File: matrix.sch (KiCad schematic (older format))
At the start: 134 parts, among them SW1 SW_Push, SW10 SW_Push, SW11 SW_Push, SW12 SW_Push, SW13 SW_Push, SW14 SW_Push, SW15 SW_Push, SW16 SW_Push, SW17 SW_Push, SW18 SW_Push, SW19 SW_Push, SW2 SW_Push, SW20 SW_Push, SW21 SW_Push, SW22 SW_Push, SW23 SW_Push, SW24 SW_Push, SW25 SW_Push, SW26 SW_Push, SW27 SW_Push, SW28 SW_Push, SW29 SW_Push, SW3 SW_Push, SW30 SW_Push, SW31 SW_Push, SW32 SW_Push, SW33 SW_Push, SW34 SW_Push, SW35 SW_Push, SW36 SW_Push, SW37 SW_Push, SW38 SW_Push, SW39 SW_Push, SW4 SW_Push, SW40 SW_Push, SW41 SW_Push, SW42 SW_Push, SW43 SW_Push, SW44 SW_Push, SW45 SW_Push, SW46 SW_Push, SW47 SW_Push, SW48 SW_Push, SW49 SW_Push, SW5 SW_Push, SW50 SW_Push, SW51 SW_Push, SW52 SW_Push, SW53 SW_Push, SW54 SW_Push, SW55 SW_Push, SW56 SW_Push, SW57 SW_Push, SW58 SW_Push, SW59 SW_Push, SW6 SW_Push, SW60 SW_Push, SW61 SW_Push, SW62 SW_Push, SW63 SW_Push, SW64 SW_Push, SW65 SW_Push, SW66 SW_Push, SW67 SW_Push, SW7 SW_Push, SW8 SW_Push, SW9 SW_Push

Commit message: Initial Commit
Initial Commit
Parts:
- D1, D10, D11, D12, D13, D14, D15, D16, D17, D18, D19, D2, D20, D21, D22, D23, D24, D25, D26, D27, D28, D29, D3, D30, D31, D32, D33, D34, D35, D36, D37, D38, D39, D4, D40, D41, D42, D43, D44, D45, D46, D47, D48, D49, D5, D50, D51, D52, D53, D54, D55, D56, D57, D58, D59, D6, D60, D61, D62, D63, D64, D65, D66, D67, D7, D8, D9: footprint Diodes_SMD:D_SOD-123 -> Diode_SMD:D_SOD-123
- SW1, SW10, SW11, SW12, SW13, SW15, SW16, SW17, SW18, SW19, SW20, SW21, SW22, SW24, SW25, SW26, SW27, SW28, SW29, SW30, SW31, SW32, SW33, SW34, SW35, SW36, SW38, SW39, SW40, SW41, SW42, SW43, SW44, SW45, SW47, SW48, SW49, SW50, SW51, SW52, SW53, SW55, SW56, SW58, SW59, SW6, SW61, SW62, SW63, SW64, SW65, SW66, SW67, SW7, SW8, SW9: footprint MX_Switch:SW_Cherry_MX_1.00u_PCB -> MX_Only:MXOnly-1U-Hotswap
- SW14, SW2, SW46, SW5, SW60: footprint MX_Switch:SW_Cherry_MX_1.50u_PCB -> MX_Only:MXOnly-1.5U-Hotswap
- SW23: footprint MX_Switch:SW_Cherry_MX_2.00u_PCB_ReversedStabilizers -> MX_Only:MXOnly-2U-Hotswap-ReversedStabilizers
- SW3, SW54: footprint MX_Switch:SW_Cherry_MX_1.75u_PCB -> MX_Only:MXOnly-1.75U-Hotswap
- SW37: footprint MX_Switch:SW_Cherry_MX_2.75u_PCB_ReversedStabilizers -> MX_Only:MXOnly-2.75U-Hotswap-ReversedStabilizers
- SW4: footprint MX_Switch:SW_Cherry_MX_2.25u_PCB -> MX_Only:MXOnly-2.25U-Hotswap
- SW57: footprint MX_Switch:SW_Cherry_MX_2.25u_PCB_ReversedStabilizers -> MX_Only:MXOnly-2.25U-Hotswap-ReversedStabilizers

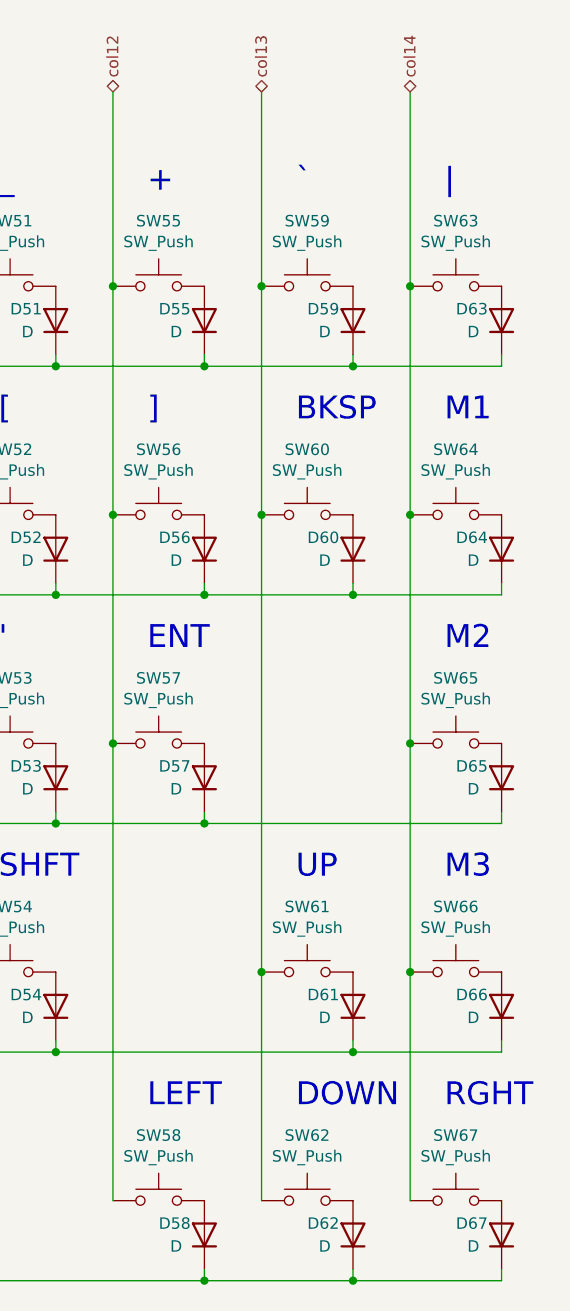
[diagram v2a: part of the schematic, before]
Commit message: Update footprints
Update backspace to 2U, left spacebar to 2.25U, left Alt to 1.25U
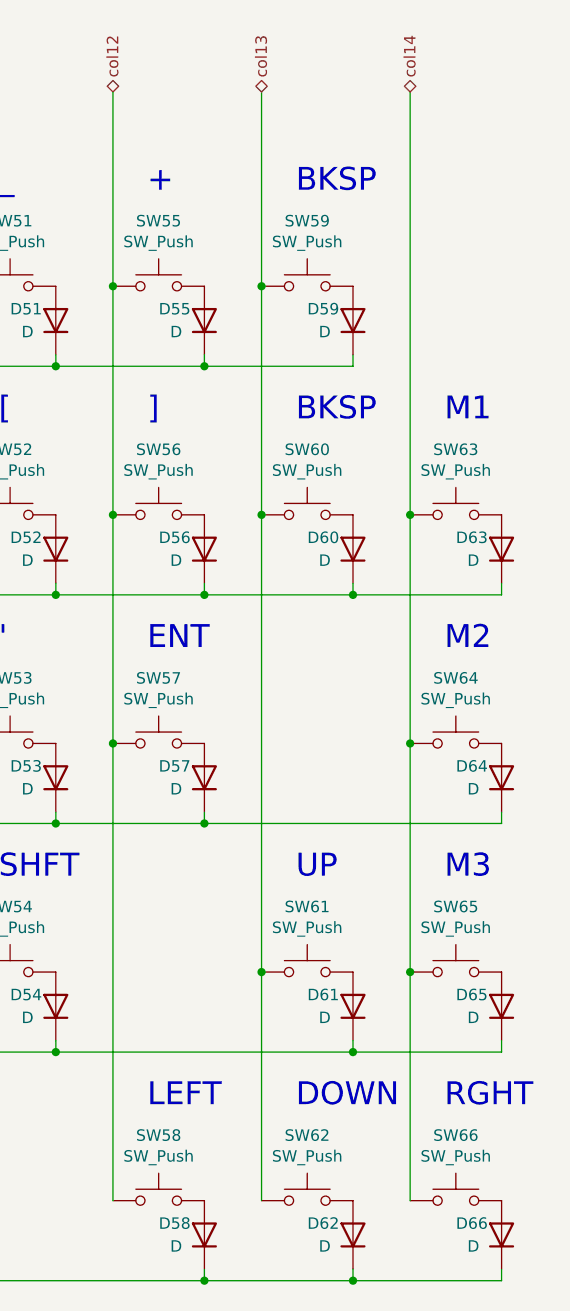
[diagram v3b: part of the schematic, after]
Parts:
- removed D63: D, Diode_SMD:D_SOD-123, symbol Device:D
- removed SW63: SW_Push, MX_Only:MXOnly-1U-Hotswap, symbol Switch:SW_Push
- SW14: footprint MX_Only:MXOnly-1.5U-Hotswap -> MX_Only:MXOnly-1.25U-Hotswap
- SW23: footprint MX_Only:MXOnly-2U-Hotswap-ReversedStabilizers -> MX_Only:MXOnly-2.25U-Hotswap-ReversedStabilizers
- SW59: footprint MX_Only:MXOnly-1U-Hotswap -> MX_Only:MXOnly-2U-Hotswap
- renumbered D64 to D63, D65 to D64, D66 to D65, D67 to D66, SW64 to SW63, SW65 to SW64, SW66 to SW65, SW67 to SW66
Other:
- note removed: "`"
- note removed: "|"
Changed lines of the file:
@@
 EESchema Schematic File Version 4
+LIBS:arisu-cache
 EELAYER 30 0
 EELAYER END
@@
 F 0 "SW14" H 2700 5885 50  0000 C CNN
 F 1 "SW_Push" H 2700 5794 50  0000 C CNN
-F 2 "MX_Only:MXOnly-1.5U-Hotswap" H 2700 5800 50  0001 C CNN
+F 2 "MX_Only:MXOnly-1.25U-Hotswap" H 2700 5800 50  0001 C CNN
 F 3 "" H 2700 5800 50  0001 C CNN
 	1    2700 5600
@@
 F 0 "SW23" H 4000 5885 50  0000 C CNN
 F 1 "SW_Push" H 4000 5794 50  0000 C CNN
-F 2 "MX_Only:MXOnly-2U-Hotswap-ReversedStabilizers" H 4000 5800 50  0001 C CNN
+F 2 "MX_Only:MXOnly-2.25U-Hotswap-ReversedStabilizers" H 4000 5800 50  0001 C CNN
 F 3 "" H 4000 5800 50  0001 C CNN
 	1    4000 5600
@@
 F 0 "SW59" H 9850 1885 50  0000 C CNN
 F 1 "SW_Push" H 9850 1794 50  0000 C CNN
-F 2 "MX_Only:MXOnly-1U-Hotswap" H 9850 1800 50  0001 C CNN
+F 2 "MX_Only:MXOnly-2U-Hotswap" H 9850 1800 50  0001 C CNN
 F 3 "" H 9850 1800 50  0001 C CNN
 	1    9850 1600
@@
 $Comp
 L Switch:SW_Push SW63
-U 1 1 5C66EC6E
-P 10500 1600
-F 0 "SW63" H 10500 1885 50  0000 C CNN
-F 1 "SW_Push" H 10500 1794 50  0000 C CNN
-F 2 "MX_Only:MXOnly-1U-Hotswap" H 10500 1800 50  0001 C CNN
-F 3 "" H 10500 1800 50  0001 C CNN
-	1    10500 1600
-	1    0    0    -1
-$EndComp
-$Comp
-L Device:D D63
-U 1 1 5C66EC76
-P 10700 1750
-F 0 "D63" V 10750 1950 50  0000 R CNN
-F 1 "D" V 10650 1900 50  0000 R CNN
-F 2 "Diode_SMD:D_SOD-123" H 10700 1750 50  0001 C CNN
-F 3 "~" H 10700 1750 50  0001 C CNN
-	1    10700 1750
-	0    -1   -1   0
-$EndComp
-$Comp
-L Switch:SW_Push SW64
 U 1 1 5C66EC7D
 P 10500 2600
-F 0 "SW64" H 10500 2885 50  0000 C CNN
+F 0 "SW63" H 10500 2885 50  0000 C CNN
 F 1 "SW_Push" H 10500 2794 50  0000 C CNN
 F 2 "MX_Only:MXOnly-1U-Hotswap" H 10500 2800 50  0001 C CNN
@@
 $EndComp
 $Comp
-L Device:D D64
+L Device:D D63
 U 1 1 5C66EC84
 P 10700 2750
-F 0 "D64" V 10750 2950 50  0000 R CNN
+F 0 "D63" V 10750 2950 50  0000 R CNN
 F 1 "D" V 10650 2900 50  0000 R CNN
 F 2 "Diode_SMD:D_SOD-123" H 10700 2750 50  0001 C CNN
@@
 	10700 2900 10700 2950
 $Comp
-L Switch:SW_Push SW65
+L Switch:SW_Push SW64
 U 1 1 5C66EC8F
 P 10500 3600
-F 0 "SW65" H 10500 3885 50  0000 C CNN
+F 0 "SW64" H 10500 3885 50  0000 C CNN
 F 1 "SW_Push" H 10500 3794 50  0000 C CNN
 F 2 "MX_Only:MXOnly-1U-Hotswap" H 10500 3800 50  0001 C CNN
@@
 $EndComp
 $Comp
-L Switch:SW_Push SW66
+L Switch:SW_Push SW65
 U 1 1 5C66EC96
 P 10500 4600
-F 0 "SW66" H 10500 4885 50  0000 C CNN
+F 0 "SW65" H 10500 4885 50  0000 C CNN
 F 1 "SW_Push" H 10500 4794 50  0000 C CNN
 F 2 "MX_Only:MXOnly-1U-Hotswap" H 10500 4800 50  0001 C CNN
@@
 	10300 4600 10300 5600
 $Comp
-L Switch:SW_Push SW67
+L Switch:SW_Push SW66
 U 1 1 5C66EC9E
 P 10500 5600
-F 0 "SW67" H 10500 5885 50  0000 C CNN
+F 0 "SW66" H 10500 5885 50  0000 C CNN
 F 1 "SW_Push" H 10500 5794 50  0000 C CNN
 F 2 "MX_Only:MXOnly-1U-Hotswap" H 10500 5800 50  0001 C CNN
@@
 $EndComp
 $Comp
-L Device:D D65
+L Device:D D64
 U 1 1 5C66ECA5
 P 10700 3750
-F 0 "D65" V 10750 3950 50  0000 R CNN
+F 0 "D64" V 10750 3950 50  0000 R CNN
 F 1 "D" V 10650 3900 50  0000 R CNN
 F 2 "Diode_SMD:D_SOD-123" H 10700 3750 50  0001 C CNN
@@
 $EndComp
 $Comp
-L Device:D D66
+L Device:D D65
 U 1 1 5C66ECAC
 P 10700 4750
-F 0 "D66" V 10750 4950 50  0000 R CNN
+F 0 "D65" V 10750 4950 50  0000 R CNN
 F 1 "D" V 10650 4900 50  0000 R CNN
 F 2 "Diode_SMD:D_SOD-123" H 10700 4750 50  0001 C CNN
@@
 $EndComp
 $Comp
-L Device:D D67
+L Device:D D66
 U 1 1 5C66ECB3
 P 10700 5750
-F 0 "D67" V 10750 5950 50  0000 R CNN
+F 0 "D66" V 10750 5950 50  0000 R CNN
 F 1 "D" V 10650 5900 50  0000 R CNN
 F 2 "Diode_SMD:D_SOD-123" H 10700 5750 50  0001 C CNN
@@
 Wire Wire Line
 	10700 3900 10700 3950
-Wire Wire Line
-	10700 1900 10700 1950
 Connection ~ 10300 4600
 Wire Wire Line
 	10300 3600 10300 4600
 Connection ~ 10300 2600
-Wire Wire Line
-	10300 1600 10300 2600
-Connection ~ 10300 1600
-Wire Wire Line
-	10300 750  10300 1600
 Text Notes 1350 1200 0    100  ~ 0
 ESC
@@
 +
 Text Notes 9800 1200 0    100  ~ 0
-`
-Text Notes 10450 1200 0    100  ~ 0
-|
+BKSP
 Text Notes 2000 2200 0    100  ~ 0
 Q
@@
 Wire Wire Line
 	9400 1950 10050 1950
-Connection ~ 10050 1950
-Wire Wire Line
-	10050 1950 10700 1950
 Wire Wire Line
 	2250 2950 2900 2950
@@
 Wire Wire Line
 	1600 5950 2900 5950
+Wire Wire Line
+	10300 750  10300 2600
 $EndSCHEMATC
